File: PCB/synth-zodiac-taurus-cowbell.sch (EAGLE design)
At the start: 53 parts, among them Q1 NPN, Q2 NPN, SW1 Push Switch, SW2 Push Switch, U1 TL071, U2 ATTiny2313, X1 16MHz, X2 16MHz

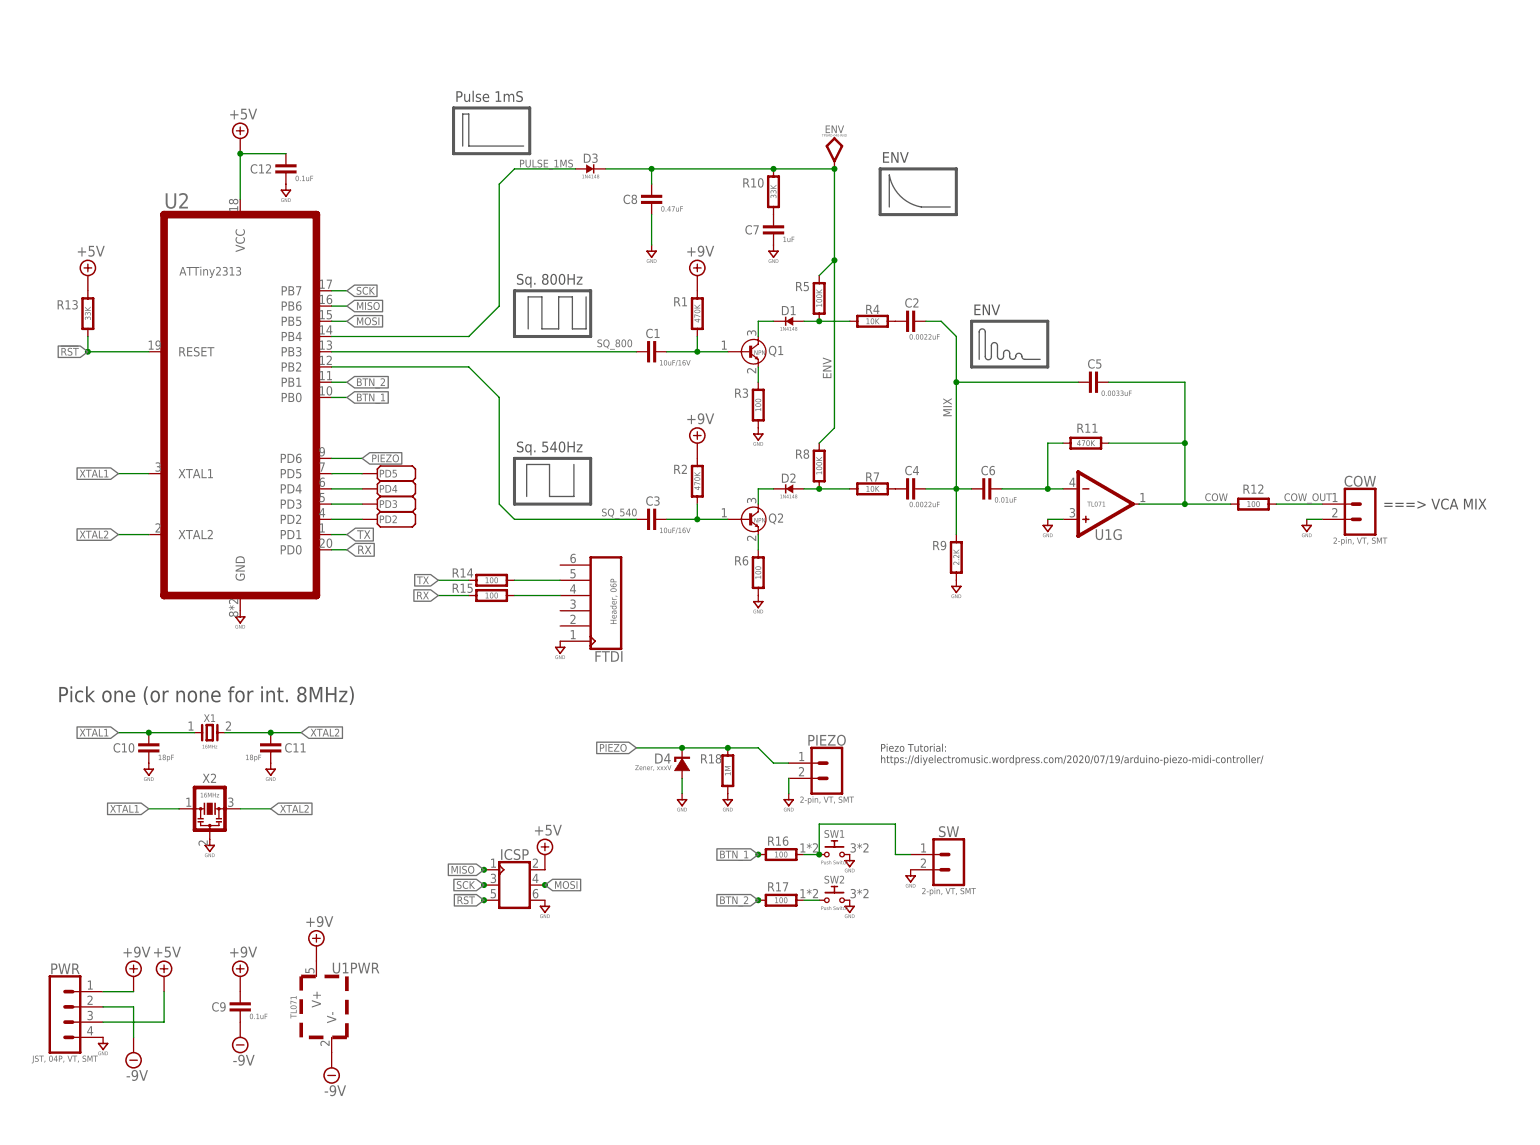
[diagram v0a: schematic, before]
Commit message: Almost ready for FAB.
Sagittarius was mis-spelled, renamed it.  Taurus is still WIP.
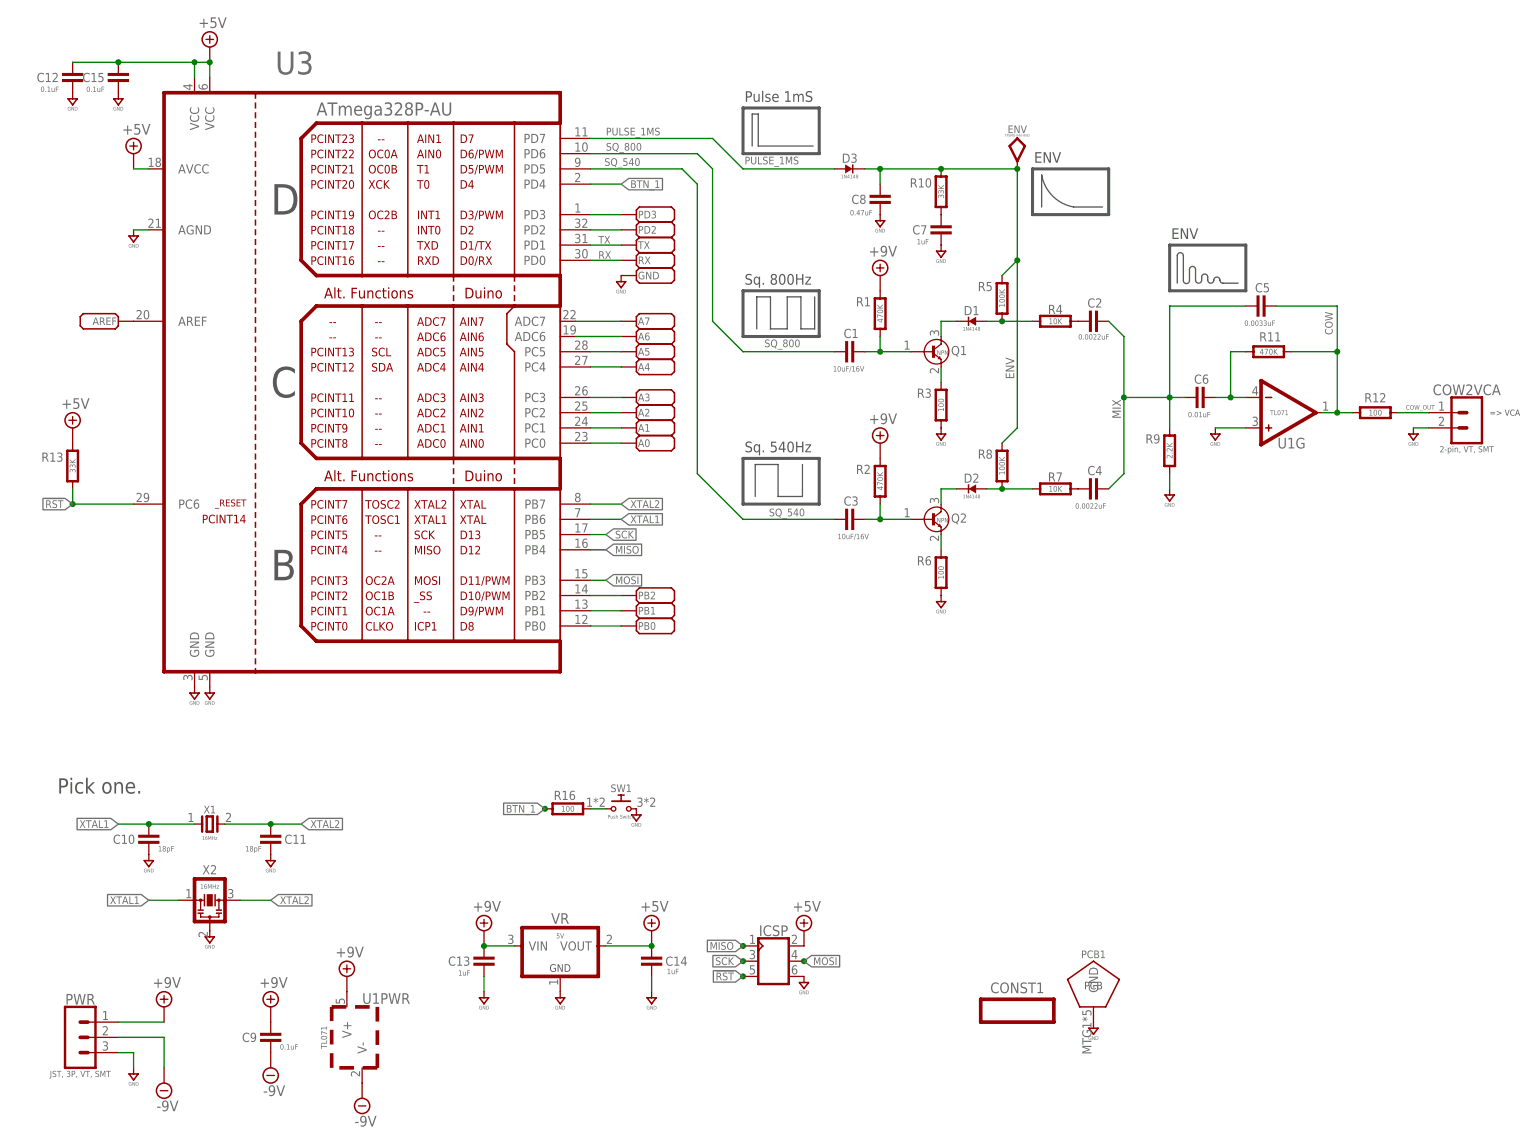
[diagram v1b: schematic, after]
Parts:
- removed COW, PIEZO, SW: 2-pin, VT, SMT, con-jst:02PVT-SMT
- removed D4: Zener, xxxV, diodes:ZENERSOT-23
- removed FTDI: Header, 06P, con-headers:CON_06X1-EDGE
- removed PD4, PD5: PADSMD-050X050, con-testpoints:PADSMD-050X050
- removed R14, R15, R17: 100, rlc:RESISTOR0603
- removed R18: 1M, rlc:RESISTOR0603
- removed SW2: Push Switch, switch-smd:PUSHBTN-MOMB3SN
- removed U2: ATTiny2313, atmel-atmega:ATTINY2313MLF
- added A0, A1, A2, A3, A4, A5, A6, A7, AREF, GND, PB0, PB1, PB2, RX, TX: PADSMD-050X050, con-testpoints:PADSMD-050X050
- added C13, C14: 1uF, rlc:CAPACITOR0603
- added C15: 0.1uF, rlc:CAPACITOR0603
- added CONST1: (no value), circuit-monkey-zodiac:CONSTELLATION-TAURUS
- added COW2VCA: 2-pin, VT, SMT, con-jst:02PVT-SMT
- added PCB1: PCB FAB, circuit-monkey-zodiac:PENTAGON-40R
- added U3: ATmega328P-AU, atmel-atmega:ATMEGA328AU
- added VR: 5V, regulators:LDO-3P--5V-SOT23
- PWR: value JST, 04P, VT, SMT -> JST, 3P, VT, SMT; device con-jst:04P-VT-SMT -> con-jst:03P-VT-SMT
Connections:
- removed net BTN_2: R17.1, U2.PB1
- removed net PIEZO: D4.K, PIEZO.1, R18.2, U2.PD6
- new net N$14: PD2.PAD, U3.PD2
- new net N$22: A3.PAD, U3.PC3
- new net N$23: A4.PAD, U3.PC4
- new net N$24: A5.PAD, U3.PC5
- new net N$25: A6.PAD, U3.ADC6
- new net N$26: A7.PAD, U3.ADC7
- new net N$27: AREF.PAD, U3.AREF
- net !RST: now also U3.PC6; no longer U2.RESET
- net +5V: now also C14.1, C15.1, U3.AVCC, U3.VCC@4, U3.VCC@6, VR.VOUT; no longer PWR.3, U2.VCC
- net +9V: now also C13.1, VR.VIN
- net BTN_1: now also U3.PD4; no longer U2.PB0
- net COW_OUT: now also COW2VCA.1; no longer COW.1
- net GND: now also C13.2, C14.2, C15.2, COW2VCA.2, GND.PAD, PCB1.GND@1, PWR.3, U3.AGND, U3.GND@3, U3.GND@5, VR.GND; no longer COW.2, D4.A, FTDI.1, PIEZO.2, PWR.4, R18.1, SW.2, SW2.2, U2.GND
- net MISO: now also U3.PB4; no longer U2.PB6
- net MOSI: now also U3.PB3; no longer U2.PB5
- net N$11: no longer SW.1
- net N$12: now also PD3.PAD, U3.PD3; no longer R17.2, SW2.1
- net N$16: now also PB2.PAD, U3.PB2; no longer PD5.PAD, U2.PD5
- net N$17: now also PB1.PAD, U3.PB1; no longer PD4.PAD, U2.PD4
- net N$18: now also PB0.PAD, U3.PB0; no longer PD3.PAD, U2.PD3
- net N$19: now also A0.PAD, U3.PC0; no longer PD2.PAD, U2.PD2
- net N$20: now also A1.PAD, U3.PC1; no longer FTDI.5, R14.2
- net N$21: now also A2.PAD, U3.PC2; no longer FTDI.4, R15.2
- net PULSE_1MS: now also U3.PD7; no longer U2.PB4
- net RX: now also RX.PAD, U3.PD0; no longer R15.1, U2.PD0
- net SCK: now also U3.PB5; no longer U2.PB7
- net SQ_540: now also U3.PD5; no longer U2.PB2
- net SQ_800: now also U3.PD6; no longer U2.PB3
- net TX: now also TX.PAD, U3.PD1; no longer R14.1, U2.PD1
- net XTAL1: now also U3.PB6; no longer U2.XTAL1
- net XTAL2: now also U3.PB7; no longer U2.XTAL2
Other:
- note added: "=> VCA"
- note added: "Pick one."
- note removed: "===> VCA MIX"
- note removed: "Pick one (or none for int. 8MHz)"
- note removed: "Piezo Tutorial: https://diyelectromusic.wordpress.com/2020/07/19/arduino-piezo-midi-controller/"
- moved on the sheet: C1, C10, C11, C12, C2, C3, C4, C5, C6, C7, C8, C9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
